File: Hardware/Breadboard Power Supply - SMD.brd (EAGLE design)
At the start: 54.6 x 16.5 mm, 25 parts, among them J1 POWER_JACKTYLERALT1, U1 V_REG_317SMD

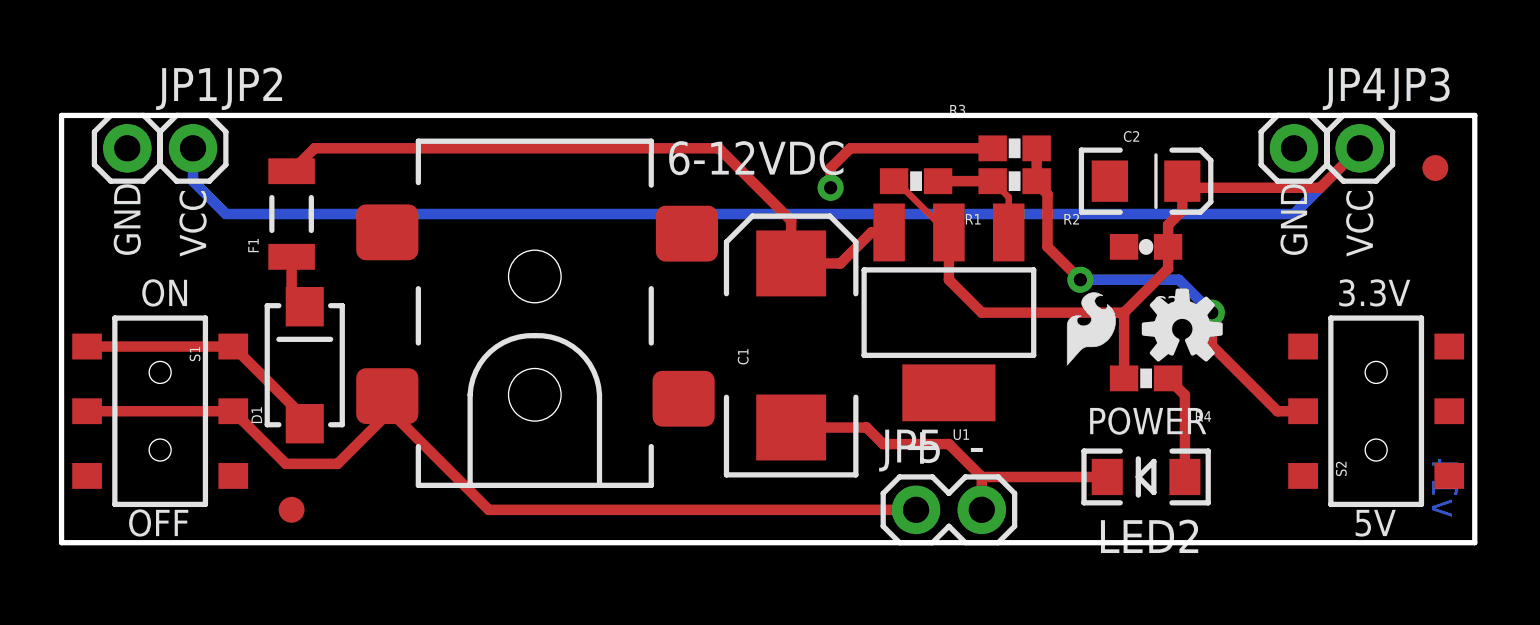
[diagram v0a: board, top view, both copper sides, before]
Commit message: Fixed Review Issues
Added extra VCC and GND headers for stability. spaced out res along top
edge. removed weird tDocu lines. cleaned up repo
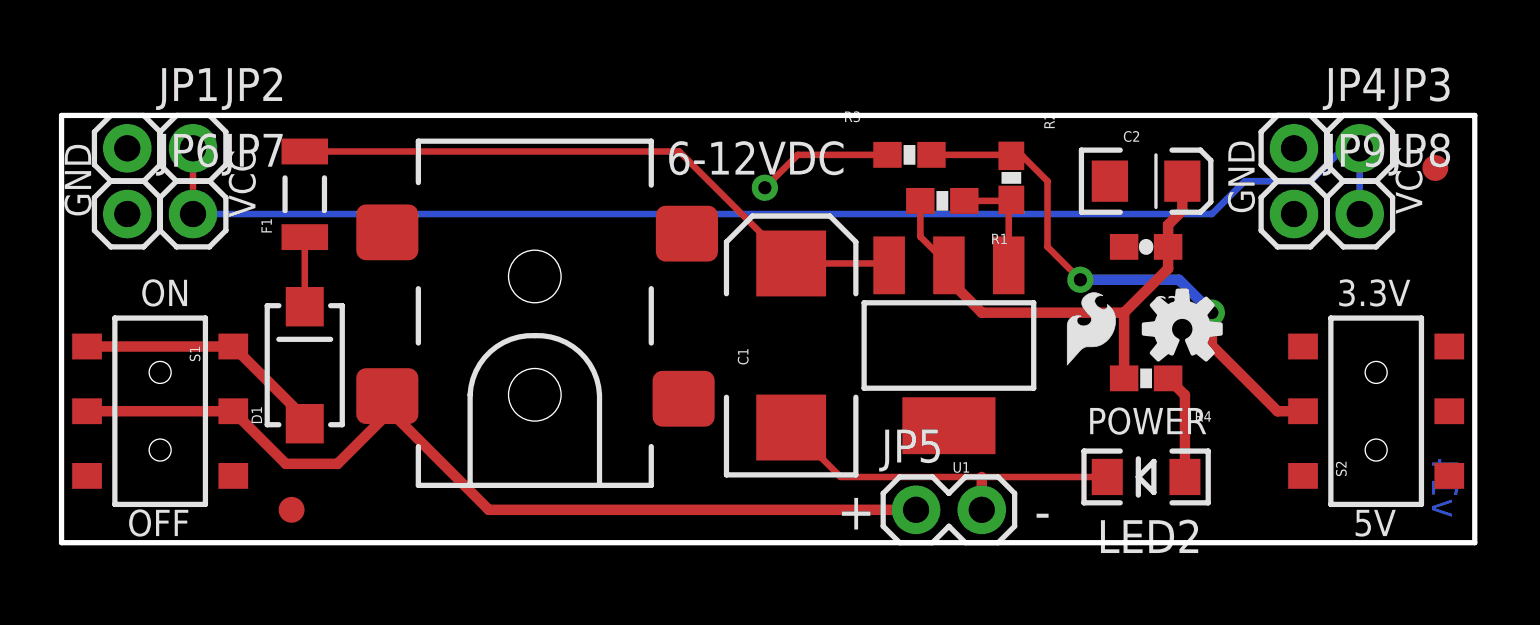
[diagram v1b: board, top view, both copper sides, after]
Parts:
- added JP6, JP7, JP8, JP9: M01PTH, SparkFun:1X01
- moved R3 4.07 mm to (32.8, 15.0)
- moved U1 1.27 mm to (34.3, 7.62)
- moved R1 1.27 mm to (34.0, 13.2)
- moved F1 0.92 mm to (9.40, 13.5)
- moved R2 0.18 mm to (36.7, 14.1), turned to 270 degrees
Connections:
- net GND: now also JP6.1, JP9.1
- net VCC: now also JP7.1, JP8.1
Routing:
- net VCC: track 76.3 -> 71.1 mm
- net N$4: track 17.4 -> 20.7 mm
- net RAW: track 26.8 -> 24.4 mm
- net GND: track 21.6 -> 19.5 mm
- net N$1: track 2.14 -> 2.69 mm

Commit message: Updated Footprints
Updated footprints on the Diode/PTC/BarrelJack
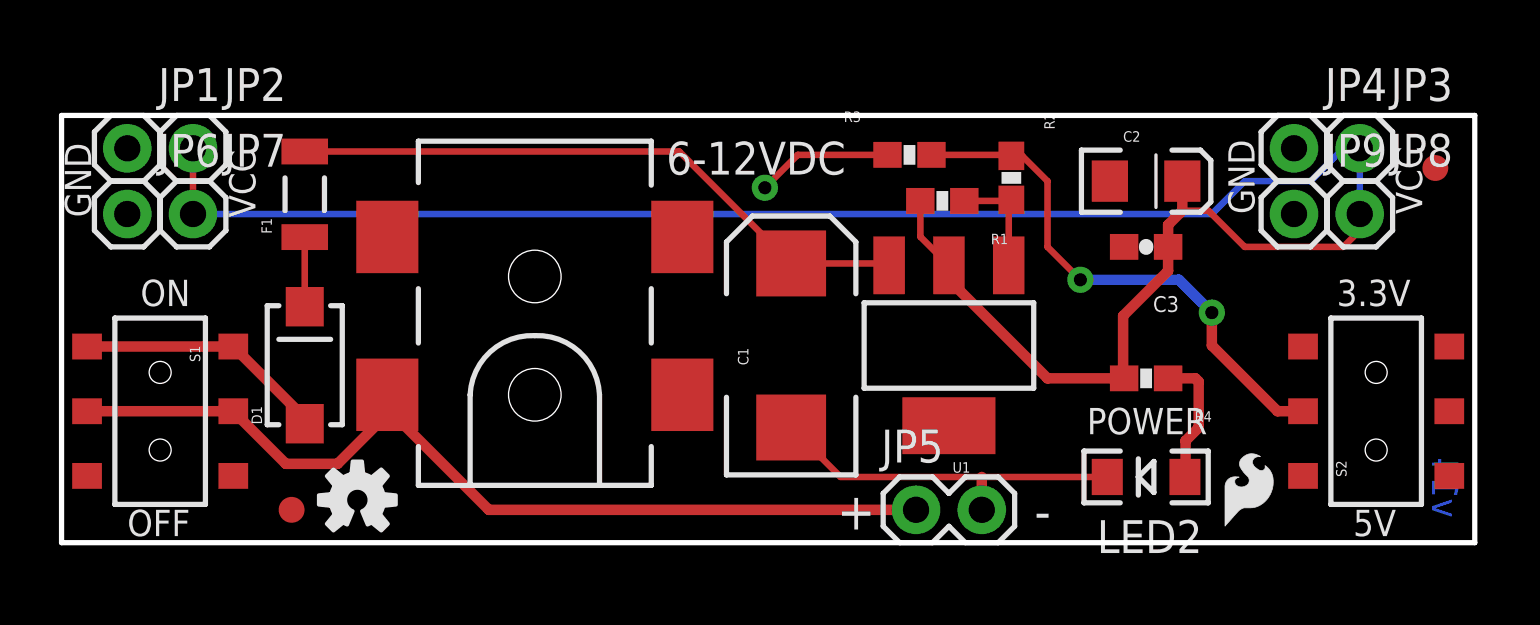
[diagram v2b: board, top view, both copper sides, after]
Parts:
- F1: value PTCWIDE -> PTCSMD-W; device Testing:PTC-1206-WIDE -> SparkFun-PowerIC:PTC-1206-WIDE
- J1: value POWER_JACKTYLERALT1 -> POWER_JACKSMD; device Testing:POWER_JACK_SMD_TYLERALT1 -> SparkFun-Connectors:POWER_JACK_SMD
- moved LOGO1 32.6 mm to (11.4, 1.65)
- moved U$1 8.71 mm to (45.0, 0.64)
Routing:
- net VCC: track 71.1 -> 80.5 mm
- net N$8: track 4.37 -> 5.43 mm
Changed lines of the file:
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@@
 <layer number="47" name="Measures" color="7" fill="1" visible="no" active="yes"/>
 <layer number="48" name="Document" color="7" fill="1" visible="no" active="yes"/>
-<layer number="49" name="Reference" color="7" fill="1" visible="yes" active="yes"/>
+<layer number="49" name="Reference" color="7" fill="1" visible="no" active="yes"/>
 <layer number="50" name="dxf" color="7" fill="1" visible="no" active="yes"/>
 <layer number="51" name="tDocu" color="6" fill="1" visible="yes" active="yes"/>
@@
 <text x="1.143" y="12.573" size="1.016" layer="21" ratio="15" rot="R90">GND</text>
 <text x="7.493" y="12.573" size="1.016" layer="21" ratio="15" rot="R90">VCC</text>
-<text x="53.975" y="3.302" size="1.016" layer="16" font="vector" ratio="25" rot="MR270">v14</text>
+<text x="53.975" y="3.302" size="1.016" layer="16" font="vector" ratio="16" rot="MR270">v14</text>
 <text x="-76.2" y="0" size="1.778" layer="27" font="vector" ratio="15">N. Seidle</text>
 <text x="-96.52" y="-2.54" size="1.778" layer="27" font="vector" ratio="15">Revised By: T Talmage</text>
@@
 </element>
 <element name="U1" library="SparkFun" package="SOT223" value="V_REG_317SMD" x="34.29" y="7.62" rot="R180"/>
-<element name="F1" library="Testing" package="PTC-1206-WIDE" value="PTCWIDE" x="9.398" y="13.462" rot="R90"/>
+<element name="F1" library="SparkFun-PowerIC" package="PTC-1206-WIDE" value="PTCSMD-W" x="9.398" y="13.462" rot="R90"/>
 <element name="JP1" library="SparkFun" package="1X01" value="M01PTH" x="2.54" y="15.24"/>
 <element name="JP2" library="SparkFun" package="1X01" value="M01PTH" x="5.08" y="15.24"/>
 <element name="JP3" library="SparkFun" package="1X01" value="M01PTH" x="50.165" y="15.24"/>
 <element name="JP4" library="SparkFun" package="1X01" value="M01PTH" x="47.625" y="15.24"/>
-<element name="U$1" library="SparkFun" package="SFE-LOGO-FLAME" value="LOGO-SFESK" x="38.862" y="6.858"/>
-<element name="J1" library="Testing" package="POWER_JACK_SMD_TYLERALT1" value="POWER_JACKTYLERALT1" x="18.288" y="5.715" rot="R90"/>
+<element name="U$1" library="SparkFun" package="SFE-LOGO-FLAME" value="LOGO-SFESK" x="44.958" y="0.635"/>
+<element name="J1" library="SparkFun-Connectors" package="POWER_JACK_SMD" value="POWER_JACKSMD" x="18.288" y="5.715" rot="R90">
+<attribute name="PROD_ID" value="CONN-08106" x="18.288" y="5.715" size="1.778" layer="27" rot="R90" display="off"/>
+<attribute name="VALUE" value="5.5x2.1mm Barrel" x="18.288" y="5.715" size="1.778" layer="27" rot="R90" display="off"/>
+</element>
 <element name="JP5" library="SparkFun" package="1X02" value="" x="33.02" y="1.27"/>
 <element name="D1" library="Testing" package="SMA-DIODE-TYLERALT1" value="1N4001" x="9.398" y="6.858" rot="R90"/>
@@
 <element name="U$3" library="SparkFun" package="FIDUCIAL-1X2" value="FIDUCIAL1X2" x="8.89" y="1.27"/>
 <element name="U$4" library="SparkFun" package="FIDUCIAL-1X2" value="FIDUCIAL1X2" x="53.086" y="14.478"/>
-<element name="LOGO1" library="SparkFun-Aesthetics" package="OSHW-LOGO-S" value="OSHW-LOGOS" x="43.307" y="8.255"/>
+<element name="LOGO1" library="SparkFun-Aesthetics" package="OSHW-LOGO-S" value="OSHW-LOGOS" x="11.43" y="1.651"/>
 <element name="FRAME1" library="SparkFun-Aesthetics" package="CREATIVE_COMMONS" value="FRAME-LETTER" x="-107.422121875" y="0"/>
 <element name="JP6" library="SparkFun" package="1X01" value="M01PTH" x="2.54" y="12.7"/>
@@
 <contactref element="R4" pad="1"/>
 <wire x1="42.76" y1="6.35" x2="43.053" y2="6.35" width="0.4064" layer="1"/>
-<wire x1="43.41" y1="5.7" x2="43.41" y2="2.54" width="0.4064" layer="1"/>
-<wire x1="42.76" y1="6.35" x2="43.41" y2="5.7" width="0.4064" layer="1"/>
+<wire x1="42.76" y1="6.35" x2="43.815" y2="6.35" width="0.4064" layer="1"/>
+<wire x1="43.815" y1="6.35" x2="43.942" y2="6.223" width="0.4064" layer="1"/>
+<wire x1="43.942" y1="6.223" x2="43.942" y2="4.445" width="0.4064" layer="1"/>
+<wire x1="43.942" y1="4.445" x2="43.434" y2="3.937" width="0.4064" layer="1"/>
+<wire x1="43.434" y1="3.937" x2="43.434" y2="2.564" width="0.4064" layer="1"/>
+<wire x1="43.434" y1="2.564" x2="43.41" y2="2.54" width="0.4064" layer="1"/>
 </signal>
 <signal name="RAW">
@@
 <wire x1="43.31" y1="13.97" x2="43.18" y2="13.97" width="0.4064" layer="1"/>
 <wire x1="34.29" y1="10.16" x2="34.29" y2="10.7188" width="0.4064" layer="1"/>
-<wire x1="35.56" y1="8.89" x2="34.29" y2="10.16" width="0.4064" layer="1"/>
 <wire x1="43.564" y1="13.716" x2="43.31" y2="13.97" width="0.4064" layer="1" curve="-90"/>
-<wire x1="41.06" y1="8.89" x2="41.06" y2="6.35" width="0.4064" layer="1"/>
-<wire x1="41.06" y1="8.89" x2="35.56" y2="8.89" width="0.4064" layer="1"/>
-<wire x1="42.76" y1="10.59" x2="41.06" y2="8.89" width="0.4064" layer="1"/>
-<wire x1="42.76" y1="11.43" x2="42.76" y2="10.59" width="0.4064" layer="1"/>
 <wire x1="42.76" y1="12.28" x2="42.76" y2="11.43" width="0.4064" layer="1"/>
 <wire x1="43.31" y1="12.83" x2="42.76" y2="12.28" width="0.4064" layer="1"/>
@@
 <wire x1="33.186" y1="11.8228" x2="34.29" y2="10.7188" width="0.254" layer="1"/>
 <wire x1="50.165" y1="12.7" x2="50.165" y2="15.24" width="0.254" layer="16"/>
-<wire x1="44.45" y1="12.7" x2="43.31" y2="12.83" width="0" layer="19" extent="1-16"/>
+<wire x1="43.31" y1="12.83" x2="44.32" y2="12.83" width="0.254" layer="1"/>
+<wire x1="44.32" y1="12.83" x2="45.72" y2="11.43" width="0.254" layer="1"/>
+<wire x1="45.72" y1="11.43" x2="49.53" y2="11.43" width="0.254" layer="1"/>
+<wire x1="49.53" y1="11.43" x2="50.165" y2="12.065" width="0.254" layer="1"/>
+<wire x1="50.165" y1="12.065" x2="50.165" y2="12.7" width="0.254" layer="1"/>
+<wire x1="34.29" y1="10.16" x2="38.1" y2="6.35" width="0.4064" layer="1"/>
+<wire x1="38.1" y1="6.35" x2="41.06" y2="6.35" width="0.4064" layer="1"/>
+<wire x1="42.76" y1="11.43" x2="42.76" y2="10.502" width="0.4064" layer="1"/>
+<wire x1="42.76" y1="10.502" x2="41.021" y2="8.763" width="0.4064" layer="1"/>
+<wire x1="41.021" y1="8.763" x2="41.021" y2="6.389" width="0.4064" layer="1"/>
+<wire x1="41.021" y1="6.389" x2="41.06" y2="6.35" width="0.4064" layer="1"/>
 </signal>
 <signal name="N$1">
@@
 <wire x1="10.668" y1="3.048" x2="12.7" y2="5.08" width="0.4064" layer="1"/>
 <wire x1="12.7" y1="5.08" x2="16.51" y2="1.27" width="0.4064" layer="1"/>
-<wire x1="12.588" y1="5.6642" x2="12.588" y2="5.192" width="0.4064" layer="1"/>
+<wire x1="12.588" y1="5.715" x2="12.588" y2="5.192" width="0.4064" layer="1"/>
 <wire x1="12.588" y1="5.192" x2="12.7" y2="5.08" width="0.4064" layer="1"/>
 </signal>
@@
 </signal>
 </signals>
-<errors>
-</errors>
 </board>
 </drawing>
